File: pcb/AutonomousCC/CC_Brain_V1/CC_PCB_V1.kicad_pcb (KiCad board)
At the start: 2 copper layers, 104.2 x 144.9 mm, 33 parts, among them J1 Screw_Terminal_01x07, J2 Antenna_Conn_02x04_Odd_Even, J3 USB1130-15-A_REVA, J4 Conn_01x02_Male, J5 Relay_Conn_01x06, J6 Conn_01x02_Male, J7 Linear Actuator Power, J8 Linear Actuator, J9 Conn_01x02_Male, K1 FINDER-40.11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

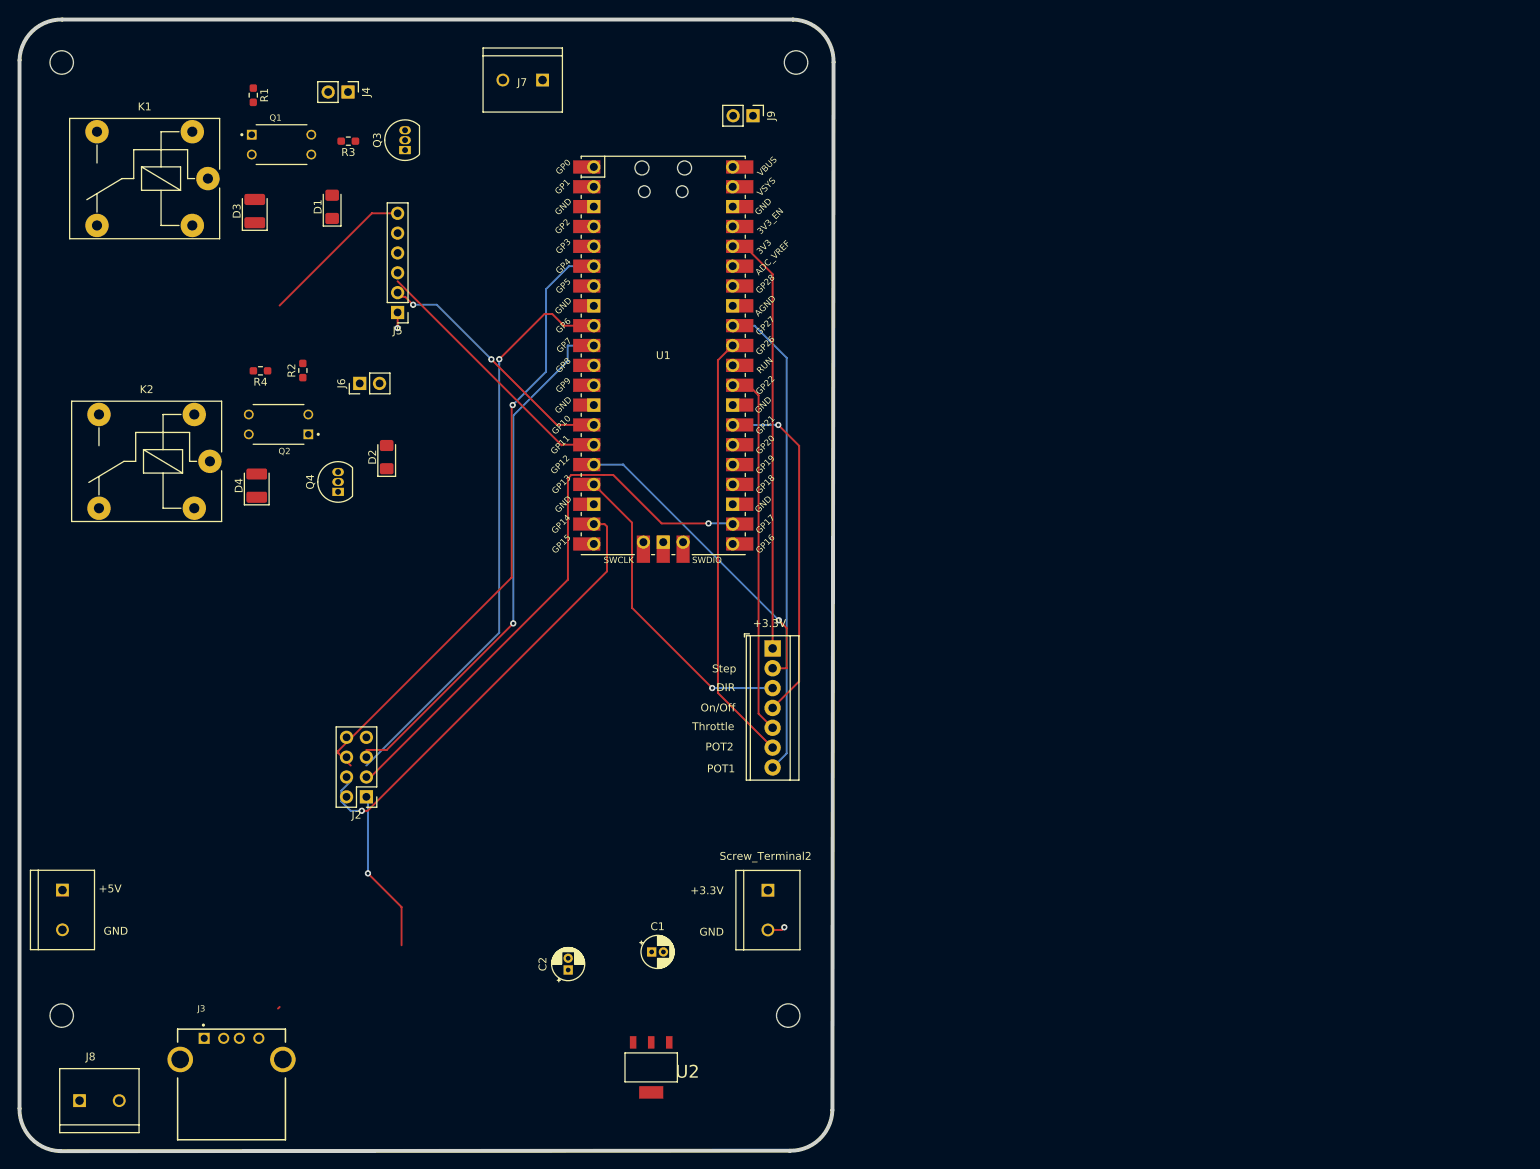
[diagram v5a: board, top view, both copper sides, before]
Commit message: Finished PCB tracing
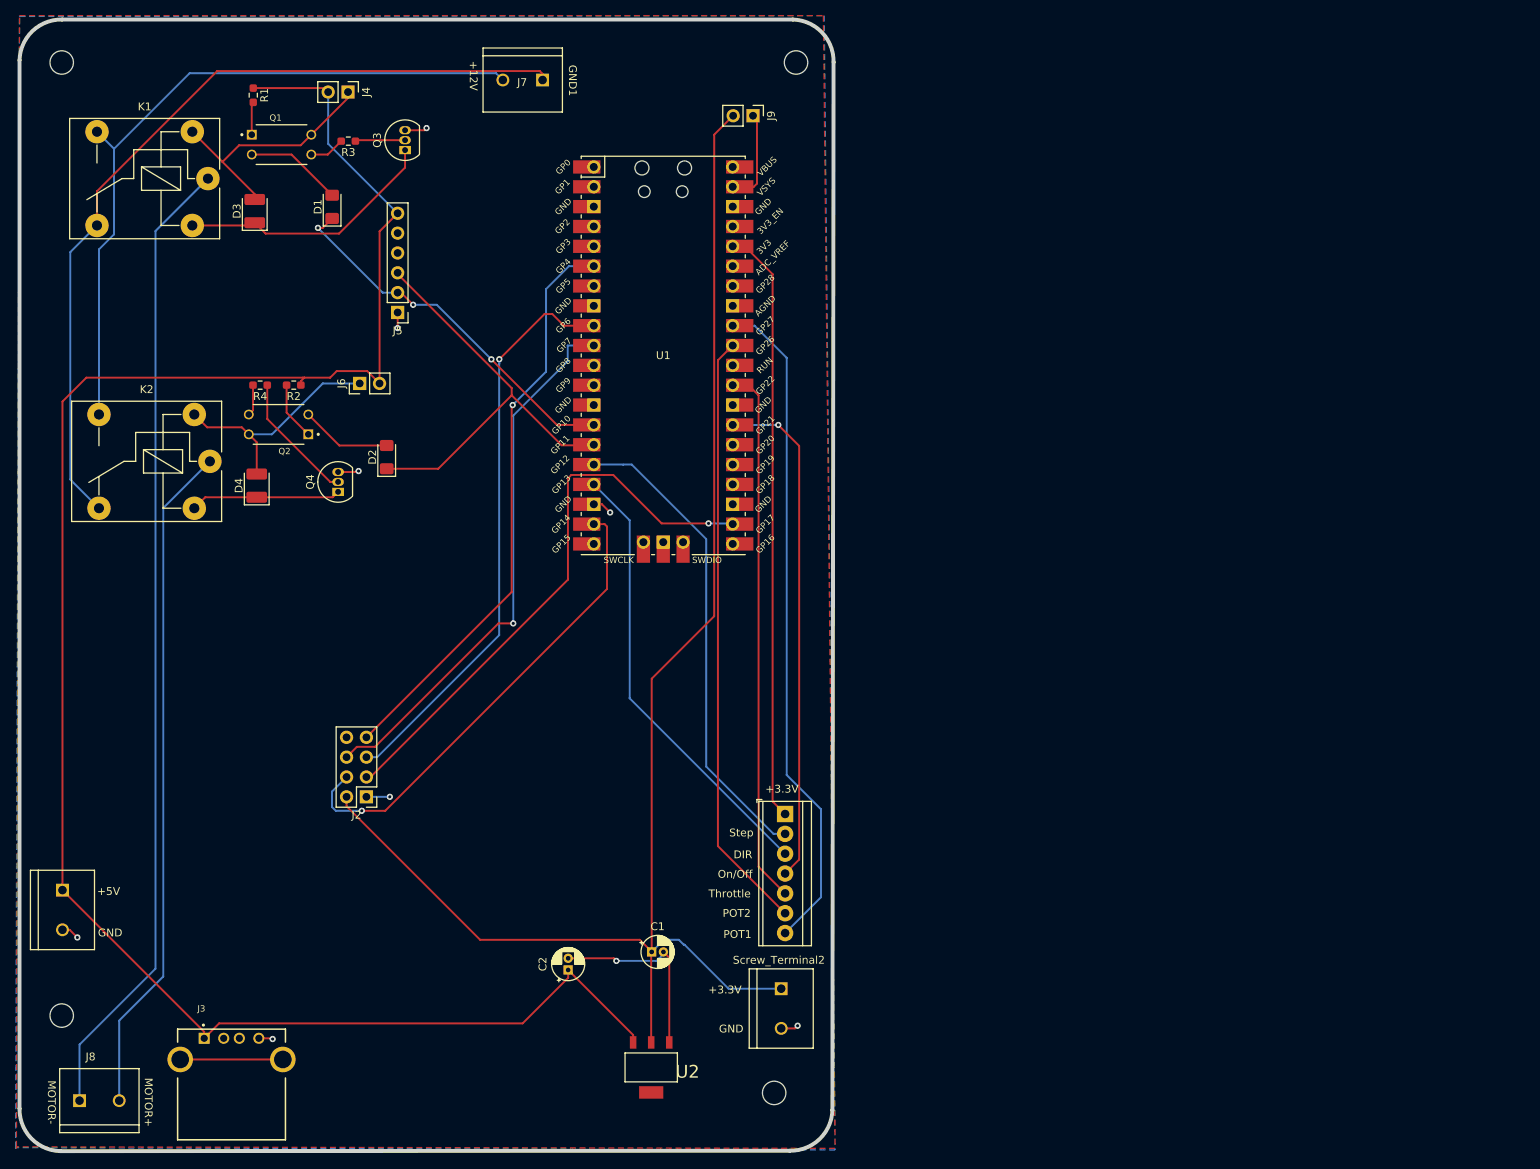
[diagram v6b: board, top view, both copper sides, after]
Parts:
- moved J1 21.3 mm to (152.6, 118.2)
- moved Screw_Terminal2 12.7 mm to (152.1, 143.1)
- moved H4 10.1 mm to (151.2, 153.9)
- moved R2 2.21 mm to (89.7, 63.3), turned to 180 degrees
- moved R4 1.83 mm to (85.4, 63.3)
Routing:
- net +5V: track 20.3 -> 248.3 mm
- net +3.3V: track 0.00 -> 190.8 mm
- net Motor-: track 0.00 -> 124.8 mm
- net GND1: track 0.00 -> 108.1 mm
- net +12V: track 0.00 -> 92.0 mm
- net Motor+: track 0.00 -> 86.6 mm
- net Net-(D3-Pad1): track 0.00 -> 34.4 mm
- net Net-(D3-Pad2): track 0.00 -> 32.2 mm
- net Net-(D4-Pad2): track 0.00 -> 30.4 mm
- net GP27: track 61.8 -> 86.0 mm
- net GP22: track 47.1 -> 69.0 mm
- net GP26: track 55.2 -> 77.0 mm
- net 3.3V: track 54.5 -> 76.4 mm
- net GP11: track 33.8 -> 54.8 mm
- net GP12: track 41.3 -> 62.0 mm, vias 1 -> 0
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- added copper zone on B.Cu, net GND
- added copper zone on F.Cu, net GND
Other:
- board text added: "+12V"
- board text added: "GND1"
- board text added: "MOTOR+"
- board text added: "MOTOR-"
